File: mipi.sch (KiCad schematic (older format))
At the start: 4 parts, among them Q1101 FDV301N, Q1102 FDV301N

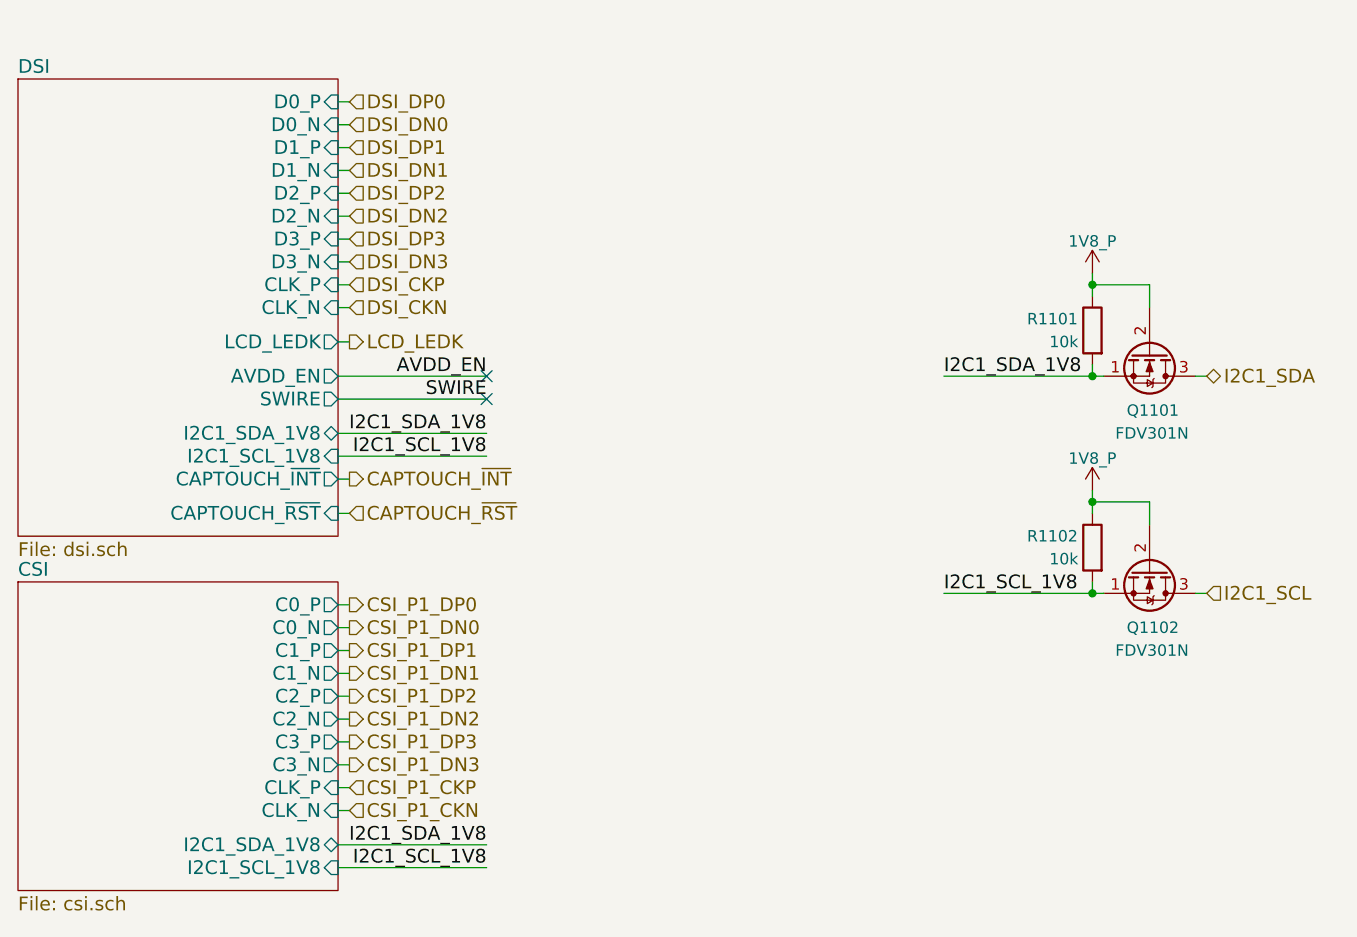
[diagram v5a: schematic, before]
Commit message: Nearly complete the LCD/DSI and cap-touch schematic, add notes from the display's datasheet regarding the various pin assignments, add component property information for the 39-pin DSI clamshell connector
Still need to determine what this requested "low power state signal" requirement is for the display.
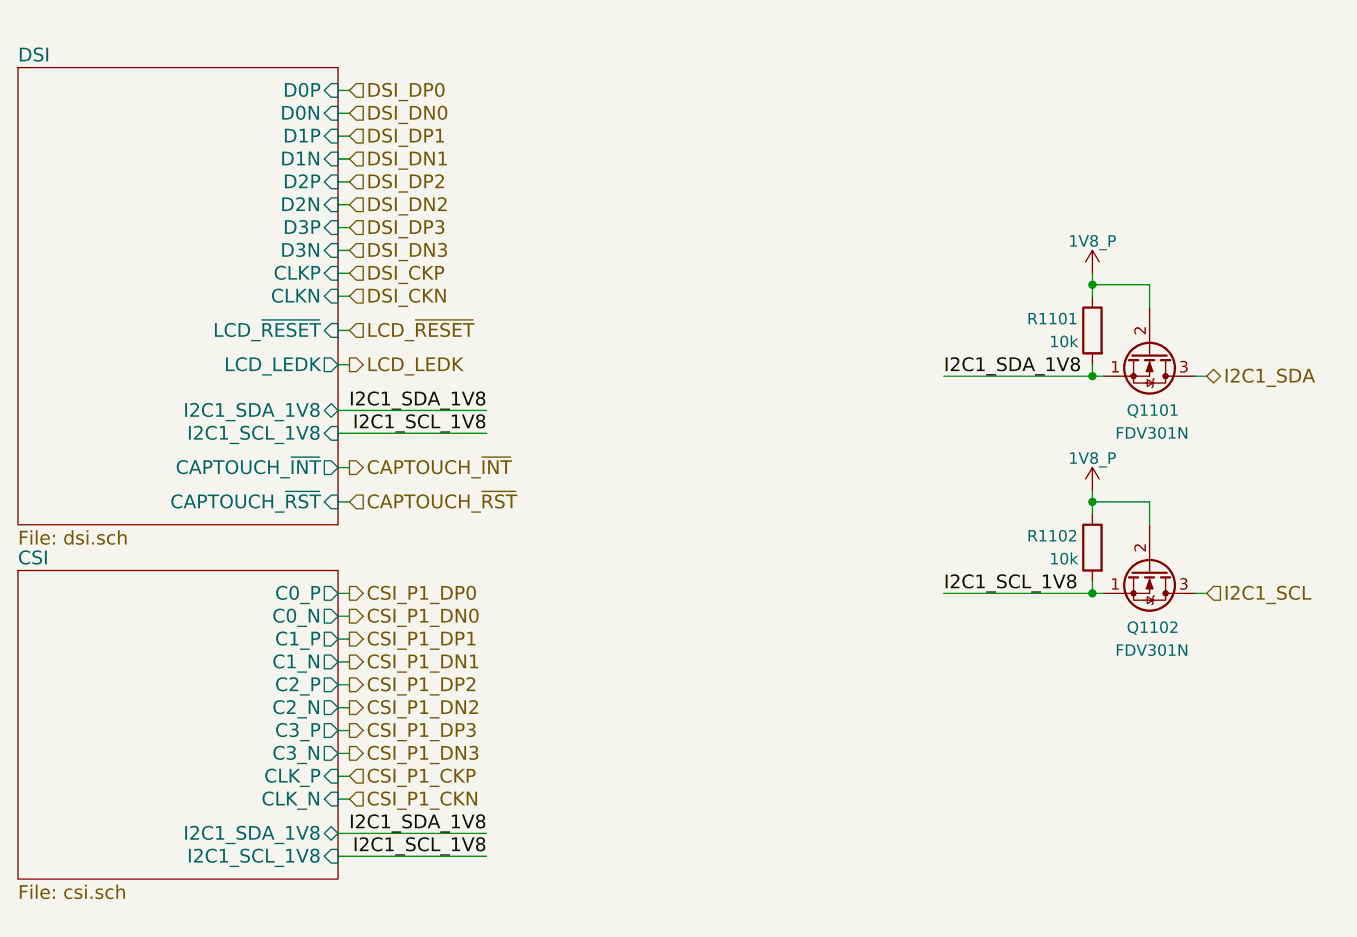
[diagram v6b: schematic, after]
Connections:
- no-connect marks 2 -> 0
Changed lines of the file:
@@
 $EndDescr
 $Sheet
-S 3000 2000 1400 2000
+S 3000 1950 1400 2000
 U 5B12DFA8
 F0 "DSI" 60
 F1 "dsi.sch" 60
-F2 "D2_P" I R 4400 2500 60
-F3 "D2_N" I R 4400 2600 60
-F4 "D1_P" I R 4400 2300 60
-F5 "D1_N" I R 4400 2400 60
-F6 "CLK_P" I R 4400 2900 60
-F7 "CLK_N" I R 4400 3000 60
-F8 "D0_P" I R 4400 2100 60
-F9 "D0_N" I R 4400 2200 60
-F10 "D3_P" I R 4400 2700 60
-F11 "D3_N" I R 4400 2800 60
-F12 "CAPTOUCH_~INT" O R 4400 3750 60
-F13 "CAPTOUCH_~RST" I R 4400 3900 60
-F14 "AVDD_EN" O R 4400 3300 60
-F15 "SWIRE" O R 4400 3400 60
-F16 "I2C1_SDA_1V8" B R 4400 3550 60
-F17 "I2C1_SCL_1V8" I R 4400 3650 60
-F18 "LCD_LEDK" O R 4400 3150 60
+F2 "CAPTOUCH_~INT" O R 4400 3700 60
+F3 "CAPTOUCH_~RST" I R 4400 3850 60
+F4 "I2C1_SDA_1V8" B R 4400 3450 60
+F5 "I2C1_SCL_1V8" I R 4400 3550 60
+F6 "LCD_LEDK" O R 4400 3250 60
+F7 "D2P" I R 4400 2450 60
+F8 "D2N" I R 4400 2550 60
+F9 "D1P" I R 4400 2250 60
+F10 "D1N" I R 4400 2350 60
+F11 "CLKP" I R 4400 2850 60
+F12 "CLKN" I R 4400 2950 60
+F13 "D0P" I R 4400 2050 60
+F14 "D0N" I R 4400 2150 60
+F15 "D3P" I R 4400 2650 60
+F16 "D3N" I R 4400 2750 60
+F17 "LCD_~RESET" I R 4400 3100 60
 $EndSheet
-Text Label 5050 3300 2    60   ~ 0
-AVDD_EN
-Text Label 5050 3400 2    60   ~ 0
-SWIRE
+Text Label 5050 3450 2    60   ~ 0
+I2C1_SDA_1V8
 Text Label 5050 3550 2    60   ~ 0
+I2C1_SCL_1V8
+Wire Wire Line
+	4400 4750 4450 4750
+Wire Wire Line
+	4400 5150 4450 5150
+Wire Wire Line
+	4400 5050 4450 5050
+Wire Wire Line
+	4400 4350 4450 4350
+Wire Wire Line
+	4400 4250 4450 4250
+Wire Wire Line
+	4400 4650 4450 4650
+Wire Wire Line
+	4400 4550 4450 4550
+Wire Wire Line
+	4400 4450 4450 4450
+Wire Wire Line
+	4400 4950 4450 4950
+Wire Wire Line
+	4400 4850 4450 4850
+Wire Wire Line
+	4400 3550 5050 3550
+Wire Wire Line
+	4400 3450 5050 3450
+Wire Wire Line
+	4400 2950 4450 2950
+Wire Wire Line
+	4400 2850 4450 2850
+Wire Wire Line
+	4400 2750 4450 2750
+Wire Wire Line
+	4400 2650 4450 2650
+Wire Wire Line
+	4400 2550 4450 2550
+Wire Wire Line
+	4400 2450 4450 2450
+Wire Wire Line
+	4400 2350 4450 2350
+Wire Wire Line
+	4400 2250 4450 2250
+Wire Wire Line
+	4400 2150 4450 2150
+Wire Wire Line
+	4400 2050 4450 2050
+Text HLabel 4450 2050 2    60   Input ~ 0
+DSI_DP0
+Text HLabel 4450 2250 2    60   Input ~ 0
+DSI_DP1
+Text HLabel 4450 2450 2    60   Input ~ 0
+DSI_DP2
+Text HLabel 4450 2650 2    60   Input ~ 0
+DSI_DP3
+Text HLabel 4450 2150 2    60   Input ~ 0
+DSI_DN0
+Text HLabel 4450 2350 2    60   Input ~ 0
+DSI_DN1
+Text HLabel 4450 2550 2    60   Input ~ 0
+DSI_DN2
+Text HLabel 4450 2750 2    60   Input ~ 0
+DSI_DN3
+Text HLabel 4450 4250 2    60   Output ~ 0
+CSI_P1_DP0
+Text HLabel 4450 4450 2    60   Output ~ 0
+CSI_P1_DP1
+Text HLabel 4450 4650 2    60   Output ~ 0
+CSI_P1_DP2
+Text HLabel 4450 4850 2    60   Output ~ 0
+CSI_P1_DP3
+Text HLabel 4450 4350 2    60   Output ~ 0
+CSI_P1_DN0
+Text HLabel 4450 4550 2    60   Output ~ 0
+CSI_P1_DN1
+Text HLabel 4450 4750 2    60   Output ~ 0
+CSI_P1_DN2
+Text HLabel 4450 4950 2    60   Output ~ 0
+CSI_P1_DN3
+Text HLabel 4450 2850 2    60   Input ~ 0
+DSI_CKP
+Text HLabel 4450 2950 2    60   Input ~ 0
+DSI_CKN
+Text HLabel 4450 5050 2    60   Input ~ 0
+CSI_P1_CKP
+Text HLabel 4450 5150 2    60   Input ~ 0
+CSI_P1_CKN
+Text Label 5050 5300 2    60   ~ 0
 I2C1_SDA_1V8
-Text Label 5050 3650 2    60   ~ 0
+Text Label 5050 5400 2    60   ~ 0
 I2C1_SCL_1V8
-NoConn ~ 5050 3400
-NoConn ~ 5050 3300
-Wire Wire Line
-	4400 4800 4450 4800
-Wire Wire Line
-	4400 5200 4450 5200
-Wire Wire Line
-	4400 5100 4450 5100
-Wire Wire Line
-	4400 4400 4450 4400
-Wire Wire Line
-	4400 4300 4450 4300
-Wire Wire Line
-	4400 4700 4450 4700
-Wire Wire Line
-	4400 4600 4450 4600
-Wire Wire Line
-	4400 4500 4450 4500
-Wire Wire Line
-	4400 5000 4450 5000
-Wire Wire Line
-	4400 4900 4450 4900
-Wire Wire Line
-	4400 3750 4450 3750
-Wire Wire Line
-	4400 3650 5050 3650
-Wire Wire Line
-	4400 3550 5050 3550
-Wire Wire Line
-	4400 3400 5050 3400
-Wire Wire Line
-	4400 3300 5050 3300
-Wire Wire Line
-	4400 3000 4450 3000
-Wire Wire Line
-	4400 2900 4450 2900
-Wire Wire Line
-	4400 2800 4450 2800
-Wire Wire Line
-	4400 2700 4450 2700
-Wire Wire Line
-	4400 2600 4450 2600
-Wire Wire Line
-	4400 2500 4450 2500
-Wire Wire Line
-	4400 2400 4450 2400
-Wire Wire Line
-	4400 2300 4450 2300
-Wire Wire Line
-	4400 2200 4450 2200
-Wire Wire Line
-	4400 2100 4450 2100
-Text HLabel 4450 2100 2    60   Input ~ 0
-DSI_DP0
-Text HLabel 4450 2300 2    60   Input ~ 0
-DSI_DP1
-Text HLabel 4450 2500 2    60   Input ~ 0
-DSI_DP2
-Text HLabel 4450 2700 2    60   Input ~ 0
-DSI_DP3
-Text HLabel 4450 2200 2    60   Input ~ 0
-DSI_DN0
-Text HLabel 4450 2400 2    60   Input ~ 0
-DSI_DN1
-Text HLabel 4450 2600 2    60   Input ~ 0
-DSI_DN2
-Text HLabel 4450 2800 2    60   Input ~ 0
-DSI_DN3
-Text HLabel 4450 4300 2    60   Output ~ 0
-CSI_P1_DP0
-Text HLabel 4450 4500 2    60   Output ~ 0
-CSI_P1_DP1
-Text HLabel 4450 4700 2    60   Output ~ 0
-CSI_P1_DP2
-Text HLabel 4450 4900 2    60   Output ~ 0
-CSI_P1_DP3
-Text HLabel 4450 4400 2    60   Output ~ 0
-CSI_P1_DN0
-Text HLabel 4450 4600 2    60   Output ~ 0
-CSI_P1_DN1
-Text HLabel 4450 4800 2    60   Output ~ 0
-CSI_P1_DN2
-Text HLabel 4450 5000 2    60   Output ~ 0
-CSI_P1_DN3
-Text HLabel 4450 2900 2    60   Input ~ 0
-DSI_CKP
-Text HLabel 4450 3000 2    60   Input ~ 0
-DSI_CKN
-Text HLabel 4450 5100 2    60   Input ~ 0
-CSI_P1_CKP
-Text HLabel 4450 5200 2    60   Input ~ 0
-CSI_P1_CKN
-Text Label 5050 5350 2    60   ~ 0
-I2C1_SDA_1V8
-Text Label 5050 5450 2    60   ~ 0
-I2C1_SCL_1V8
-Wire Wire Line
-	4400 5450 5050 5450
-Wire Wire Line
-	4400 5350 5050 5350
+Wire Wire Line
+	4400 5400 5050 5400
+Wire Wire Line
+	4400 5300 5050 5300
 Text HLabel 8200 3300 2    60   BiDi ~ 0
 I2C1_SDA
@@
 $EndComp
 $Comp
-L 1V8_P #PWR0172
+L 1V8_P #PWR0177
 U 1 1 5B1803EF
 P 7700 2850
-F 0 "#PWR0172" H 7700 2700 50  0001 C CNN
+F 0 "#PWR0177" H 7700 2700 50  0001 C CNN
 F 1 "1V8_P" H 7700 2990 50  0000 C CNN
 F 2 "" H 7700 2850 50  0001 C CNN
@@
 $EndComp
 $Comp
-L 1V8_P #PWR0173
+L 1V8_P #PWR0178
 U 1 1 5B180400
 P 7700 3800
-F 0 "#PWR0173" H 7700 3650 50  0001 C CNN
+F 0 "#PWR0178" H 7700 3650 50  0001 C CNN
 F 1 "1V8_P" H 7700 3940 50  0000 C CNN
 F 2 "" H 7700 3800 50  0001 C CNN
@@
 Text Label 7050 4250 0    60   ~ 0
 I2C1_SCL_1V8
-Text HLabel 4450 3750 2    60   Output ~ 0
+Text HLabel 4450 3700 2    60   Output ~ 0
 CAPTOUCH_~INT
-Text HLabel 4450 3900 2    60   Input ~ 0
+Text HLabel 4450 3850 2    60   Input ~ 0
 CAPTOUCH_~RST
 $Sheet
-S 3000 4200 1400 1350
+S 3000 4150 1400 1350
 U 5B12DFE7
 F0 "CSI" 60
 F1 "csi.sch" 60
-F2 "C0_P" O R 4400 4300 60
-F3 "C0_N" O R 4400 4400 60
-F4 "C1_P" O R 4400 4500 60
-F5 "C1_N" O R 4400 4600 60
-F6 "C2_P" O R 4400 4700 60
-F7 "C2_N" O R 4400 4800 60
-F8 "C3_P" O R 4400 4900 60
-F9 "C3_N" O R 4400 5000 60
-F10 "CLK_P" I R 4400 5100 60
-F11 "CLK_N" I R 4400 5200 60
-F12 "I2C1_SDA_1V8" B R 4400 5350 60
-F13 "I2C1_SCL_1V8" I R 4400 5450 60
+F2 "C0_P" O R 4400 4250 60
+F3 "C0_N" O R 4400 4350 60
+F4 "C1_P" O R 4400 4450 60
+F5 "C1_N" O R 4400 4550 60
+F6 "C2_P" O R 4400 4650 60
+F7 "C2_N" O R 4400 4750 60
+F8 "C3_P" O R 4400 4850 60
+F9 "C3_N" O R 4400 4950 60
+F10 "CLK_P" I R 4400 5050 60
+F11 "CLK_N" I R 4400 5150 60
+F12 "I2C1_SDA_1V8" B R 4400 5300 60
+F13 "I2C1_SCL_1V8" I R 4400 5400 60
 $EndSheet
 Wire Wire Line
-	4400 3150 4450 3150
-Text HLabel 4450 3150 2    60   Output ~ 0
+	4400 3250 4450 3250
+Text HLabel 4450 3250 2    60   Output ~ 0
 LCD_LEDK
-Wire Wire Line
-	4450 3900 4400 3900
+Text HLabel 4450 3100 2    60   Input ~ 0
+LCD_~RESET
+Wire Wire Line
+	4450 3100 4400 3100
+Wire Wire Line
+	4400 3700 4450 3700
+Wire Wire Line
+	4400 3850 4450 3850
 $EndSCHEMATC

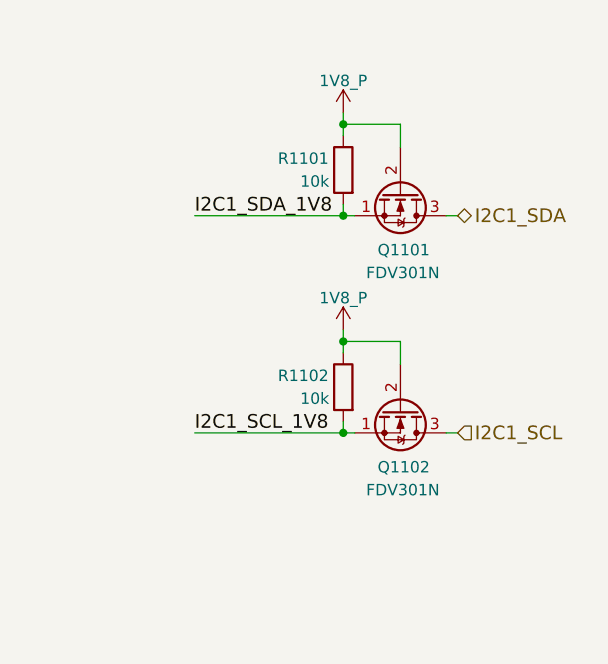
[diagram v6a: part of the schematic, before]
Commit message: Use the 2SK3018 NMOS for all low-current applications such as level-shifting
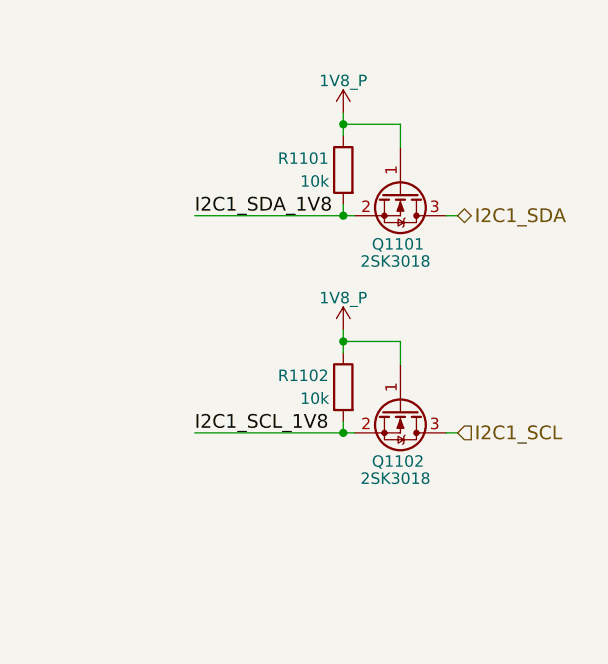
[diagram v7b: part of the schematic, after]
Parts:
- removed Q1101, Q1102: FDV301N, symbol Q_NMOS_SGD
- added Q1101, Q1102: 2SK3018, symbol Q_NMOS_GSD
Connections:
- net 1V8_P: now also Q1101.1 (G), Q1102.1 (G)
- net I2C1_SCL: now also Q1102.3 (D)
- net I2C1_SCL_1V8: now also Q1102.2 (S)
- net I2C1_SDA: now also Q1101.3 (D)
- net I2C1_SDA_1V8: now also Q1101.2 (S)
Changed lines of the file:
@@
 I2C1_SCL
-$Comp
-L Q_NMOS_SGD Q1101
-U 1 1 5B1803E8
-P 7950 3200
-F 0 "Q1101" V 8200 3100 50  0000 L CNN
-F 1 "FDV301N" V 8300 3050 50  0000 L CNN
-F 2 "" H 8150 3300 50  0001 C CNN
-F 3 "" H 7950 3200 50  0001 C CNN
-	1    7950 3200
-	0    1    1    0
-$EndComp
 $Comp
 L 1V8_P #PWR0177
@@
 	1    7700 2850
 	1    0    0    -1
-$EndComp
-$Comp
-L Q_NMOS_SGD Q1102
-U 1 1 5B1803F6
-P 7950 4150
-F 0 "Q1102" V 8200 4050 50  0000 L CNN
-F 1 "FDV301N" V 8300 4000 50  0000 L CNN
-F 2 "" H 8150 4250 50  0001 C CNN
-F 3 "" H 7950 4150 50  0001 C CNN
-	1    7950 4150
-	0    1    1    0
 $EndComp
 $Comp
@@
 Wire Wire Line
 	4400 3850 4450 3850
+$Comp
+L Q_NMOS_GSD Q1102
+U 1 1 5B58BACE
+P 7950 4150
+F 0 "Q1102" V 8175 4025 50  0000 L CNN
+F 1 "2SK3018" V 8250 3975 50  0000 L CNN
+F 2 "" H 8150 4250 50  0001 C CNN
+F 3 "http://www.mccsemi.com/up_pdf/2SK3018(SOT-323).pdf" H 7950 4150 50  0001 C CNN
+F 4 "Micro Commercial Co" V 7950 4150 60  0001 C CNN "MFG Name"
+F 5 "2SK3018-TP" V 7950 4150 60  0001 C CNN "MFG Part Num"
+F 6 "833-2SK3018-TP" V 7950 4150 60  0001 C CNN "Distrib PN"
+F 7 "https://www.mouser.com/ProductDetail/Micro-Commercial-Components-MCC/2SK3018-TP?qs=sGAEpiMZZMtI26rxh1qzjnDHXOVLFYvgyLpQIEHdJp0%3d" V 7950 4150 60  0001 C CNN "Distrib Link"
+F 8 "-" V 7950 4150 60  0001 C CNN "Tolerance"
+F 9 "https://www.digikey.com/product-detail/en/micro-commercial-co/2SK3018-TP/2SK3018-TPMSCT-ND/6616131" V 7950 4150 60  0001 C CNN "Others"
+	1    7950 4150
+	0    1    1    0
+$EndComp
+$Comp
+L Q_NMOS_GSD Q1101
+U 1 1 5B58FE44
+P 7950 3200
+F 0 "Q1101" V 8175 3075 50  0000 L CNN
+F 1 "2SK3018" V 8250 3025 50  0000 L CNN
+F 2 "" H 8150 3300 50  0001 C CNN
+F 3 "http://www.mccsemi.com/up_pdf/2SK3018(SOT-323).pdf" H 7950 3200 50  0001 C CNN
+F 4 "Micro Commercial Co" V 7950 3200 60  0001 C CNN "MFG Name"
+F 5 "2SK3018-TP" V 7950 3200 60  0001 C CNN "MFG Part Num"
+F 6 "833-2SK3018-TP" V 7950 3200 60  0001 C CNN "Distrib PN"
+F 7 "https://www.mouser.com/ProductDetail/Micro-Commercial-Components-MCC/2SK3018-TP?qs=sGAEpiMZZMtI26rxh1qzjnDHXOVLFYvgyLpQIEHdJp0%3d" V 7950 3200 60  0001 C CNN "Distrib Link"
+F 8 "-" V 7950 3200 60  0001 C CNN "Tolerance"
+F 9 "https://www.digikey.com/product-detail/en/micro-commercial-co/2SK3018-TP/2SK3018-TPMSCT-ND/6616131" V 7950 3200 60  0001 C CNN "Others"
+	1    7950 3200
+	0    1    1    0
+$EndComp
 $EndSCHEMATC
